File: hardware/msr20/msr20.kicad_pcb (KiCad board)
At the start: 2 copper layers, 0 parts

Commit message: initial board layout; dimensions
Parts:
- added U1: RF-BPF, msr20:RF-BPF, F.Cu at (198.1, 46.3)
- added U2: BGA616, msr20:BGA616, F.Cu at (187.1, 62.9)
- added U3: ADE-1+, msr20:ADE-1+, F.Cu at (189.9, 61.6)
- added U4: AD7478, Package_TO_SOT_SMD:SOT-23-6, F.Cu at (182.3, 63.3)
- added U6: 74LS163, Package_DIP:DIP-16_W7.62mm_LongPads, F.Cu at (181.7, 69.5)
- added U7: CD74HC4046, Package_DIP:DIP-16_W7.62mm_LongPads, F.Cu at (193.3, 69.5)
- added U8: NCP1117-3.3_SOT223, Package_TO_SOT_SMD:SOT-223-3_TabPin2, F.Cu at (209.8, 71.7)
- added U9: NCP1117-5.0_SOT223, Package_TO_SOT_SMD:SOT-223-3_TabPin2, F.Cu at (209.8, 80.0)
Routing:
- added copper zone on B.Cu, net GND
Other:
- board outline added: 120 x 100 mm

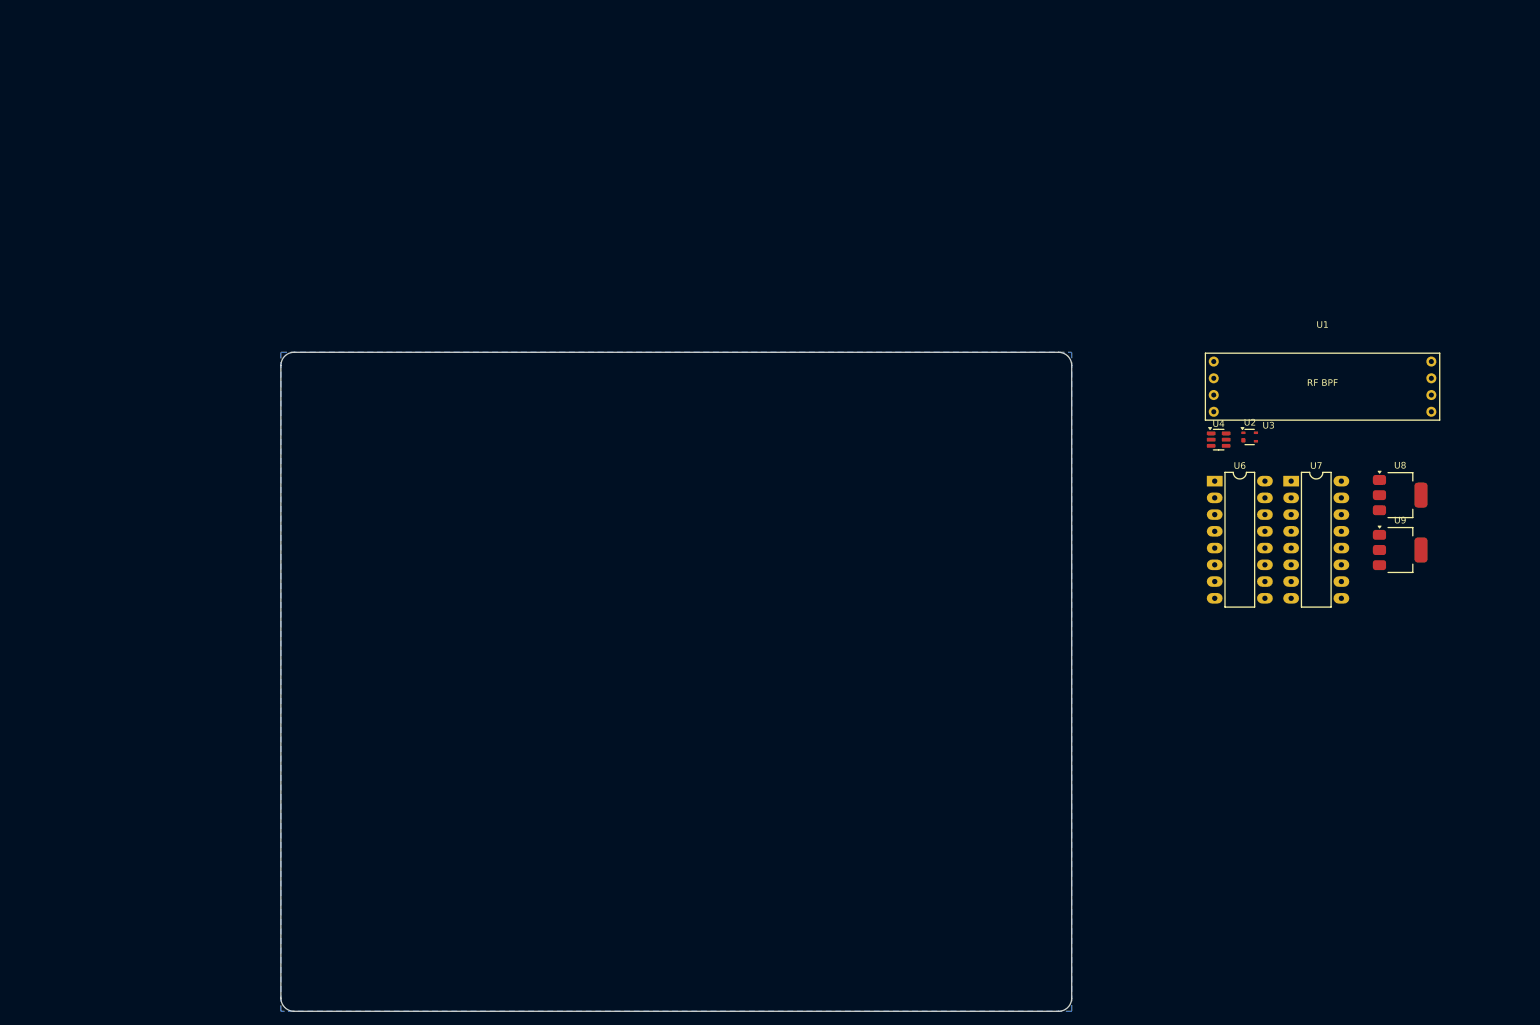
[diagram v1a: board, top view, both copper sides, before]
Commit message: rf-bpf, lna, pll, rf mixer added to pcb
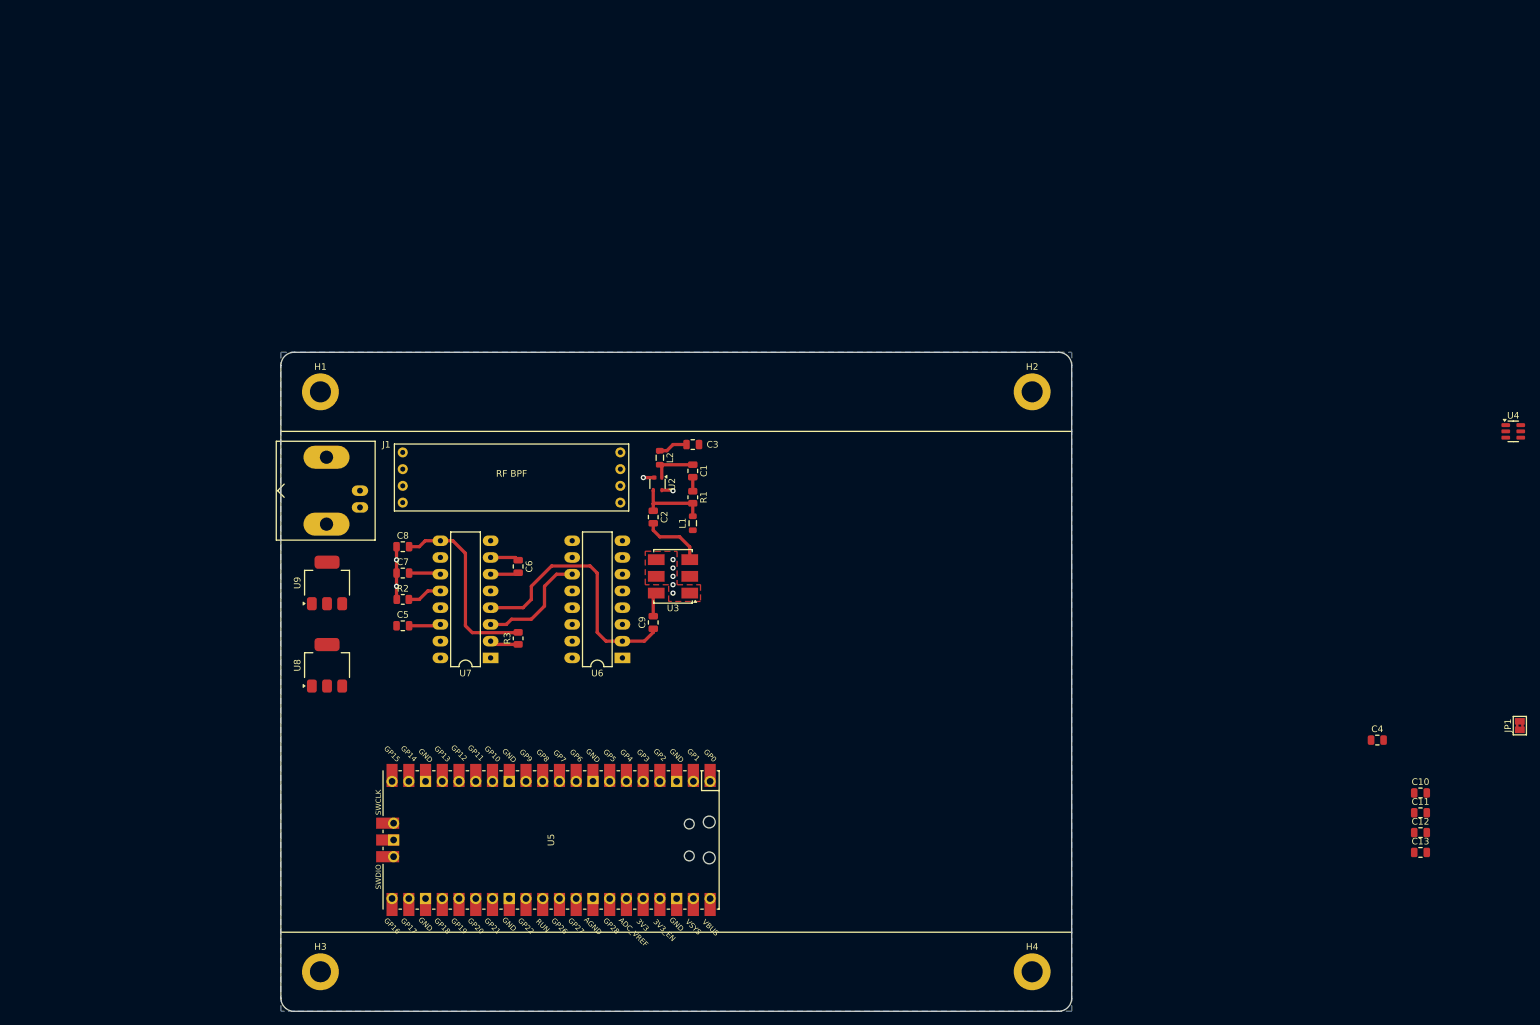
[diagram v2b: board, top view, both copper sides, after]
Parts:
- added C1: 200n, Capacitor_SMD:C_0805_2012Metric, F.Cu at (102.5, 68.0)
- added C10: 1u, Capacitor_SMD:C_0805_2012Metric, F.Cu at (212.9, 116.9)
- added C11: 1u, Capacitor_SMD:C_0805_2012Metric, F.Cu at (212.9, 119.9)
- added C12: 1u, Capacitor_SMD:C_0805_2012Metric, F.Cu at (212.9, 122.9)
- added C13: 1u, Capacitor_SMD:C_0805_2012Metric, F.Cu at (212.9, 125.9)
- added C2: 2.2u, Capacitor_SMD:C_0805_2012Metric, F.Cu at (96.5, 75.0)
- added C3: 1.5p, Capacitor_SMD:C_0805_2012Metric, F.Cu at (102.5, 64.0)
- added C4: C, Capacitor_SMD:C_0805_2012Metric, F.Cu at (206.4, 108.8)
- added C5: 1n, Capacitor_SMD:C_0805_2012Metric, F.Cu at (58.5, 91.5)
- added C6: 47p, Capacitor_SMD:C_0805_2012Metric, F.Cu at (76.0, 82.5)
- added C7: 1n, Capacitor_SMD:C_0805_2012Metric, F.Cu at (58.5, 83.5)
- added C8: 100p, Capacitor_SMD:C_0805_2012Metric, F.Cu at (58.5, 79.5)
- added C9: 1n, Capacitor_SMD:C_0805_2012Metric, F.Cu at (96.5, 91.0)
- added H1: MountingHole_Pad, MountingHole:MountingHole_3.2mm_M3_DIN965_Pad, F.Cu at (46.0, 56.0)
- added H2: MountingHole_Pad, MountingHole:MountingHole_3.2mm_M3_DIN965_Pad, F.Cu at (154.0, 56.0)
- added H3: MountingHole_Pad, MountingHole:MountingHole_3.2mm_M3_DIN965_Pad, F.Cu at (46.0, 144.0)
- added H4: MountingHole_Pad, MountingHole:MountingHole_3.2mm_M3_DIN965_Pad, F.Cu at (154.0, 144.0)
- added J1: Conn_Coaxial, Connector_Coaxial:BNC_Amphenol_B6252HB-NPP3G-50_Horizontal, F.Cu at (52.0, 71.0)
- added JP1: SolderJumper_2_Open, Jumper:SolderJumper-2_P1.3mm_Bridged2Bar_Pad1.0x1.5mm, F.Cu at (228.0, 106.7)
- added L1: 5.1n, Inductor_SMD:L_0805_2012Metric, F.Cu at (102.5, 75.9)
- added L2: 15u, Inductor_SMD:L_0805_2012Metric, F.Cu at (97.5, 66.0)
- added R1: 1.5k, Resistor_SMD:R_0805_2012Metric, F.Cu at (102.5, 72.0)
- added R2: 3.3k, Resistor_SMD:R_0805_2012Metric, F.Cu at (58.5, 87.5)
- added R3: 33k, Resistor_SMD:R_0805_2012Metric, F.Cu at (76.0, 93.4)
- added U5: Pico, MCU_RaspberryPi_and_Boards:RPi_Pico_SMD_TH, F.Cu at (81.0, 124.0)
- U3: footprint msr20:ADE-1+ -> RF_Mini-Circuits:Mini-Circuits_CD636_H4.11mm
- moved U8 164.9 mm to (47.0, 97.5), turned to 90 degrees
- moved U9 162.9 mm to (47.0, 85.0), turned to 90 degrees
- moved U7 124.4 mm to (71.8, 96.4), turned to 180 degrees
- moved U1 123.8 mm to (75.0, 60.1)
- moved U6 93.8 mm to (91.8, 96.4), turned to 180 degrees
- moved U3 93.1 mm to (99.5, 84.0), turned to 180 degrees
- moved U2 90.2 mm to (97.1, 70.0), turned to -90 degrees
- moved U4 44.7 mm to (227.0, 62.0)
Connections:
- net RF-IN renamed Net-(J1-In)
- U4 pad 3: Net-(U4-VIN) -> unconnected-(U4-VIN-Pad3)
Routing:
- net Net-(U6-CLK): track 0.00 -> 39.6 mm
- net Net-(U7-VCO-I): track 0.00 -> 29.2 mm
- net Net-(U6-Qd): track 0.00 -> 17.3 mm
- net GND: track 0.00 -> 11.4 mm, vias 0 -> 9
- net Net-(U2-OUT): track 0.00 -> 11.1 mm
- net Net-(U3-RF): track 0.00 -> 9.56 mm
- net Net-(U2-IN): track 0.00 -> 7.08 mm
- net Net-(U7-R2): track 0.00 -> 5.32 mm
- net Net-(U7-SIG): track 0.00 -> 4.84 mm
- net Net-(U7-R1): track 0.00 -> 4.83 mm
- net Net-(C3-Pad1): track 0.00 -> 4.80 mm
- net Net-(U7-PC1): track 0.00 -> 4.38 mm
- net Net-(U7-C1B): track 0.00 -> 4.35 mm
- net Net-(U7-C1A): track 0.00 -> 4.27 mm
- net /Phase-Locked Loop/PLL-OUT: track 0.00 -> 3.76 mm
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- added copper zone on F.Cu, net GND

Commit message: add if section to pcb
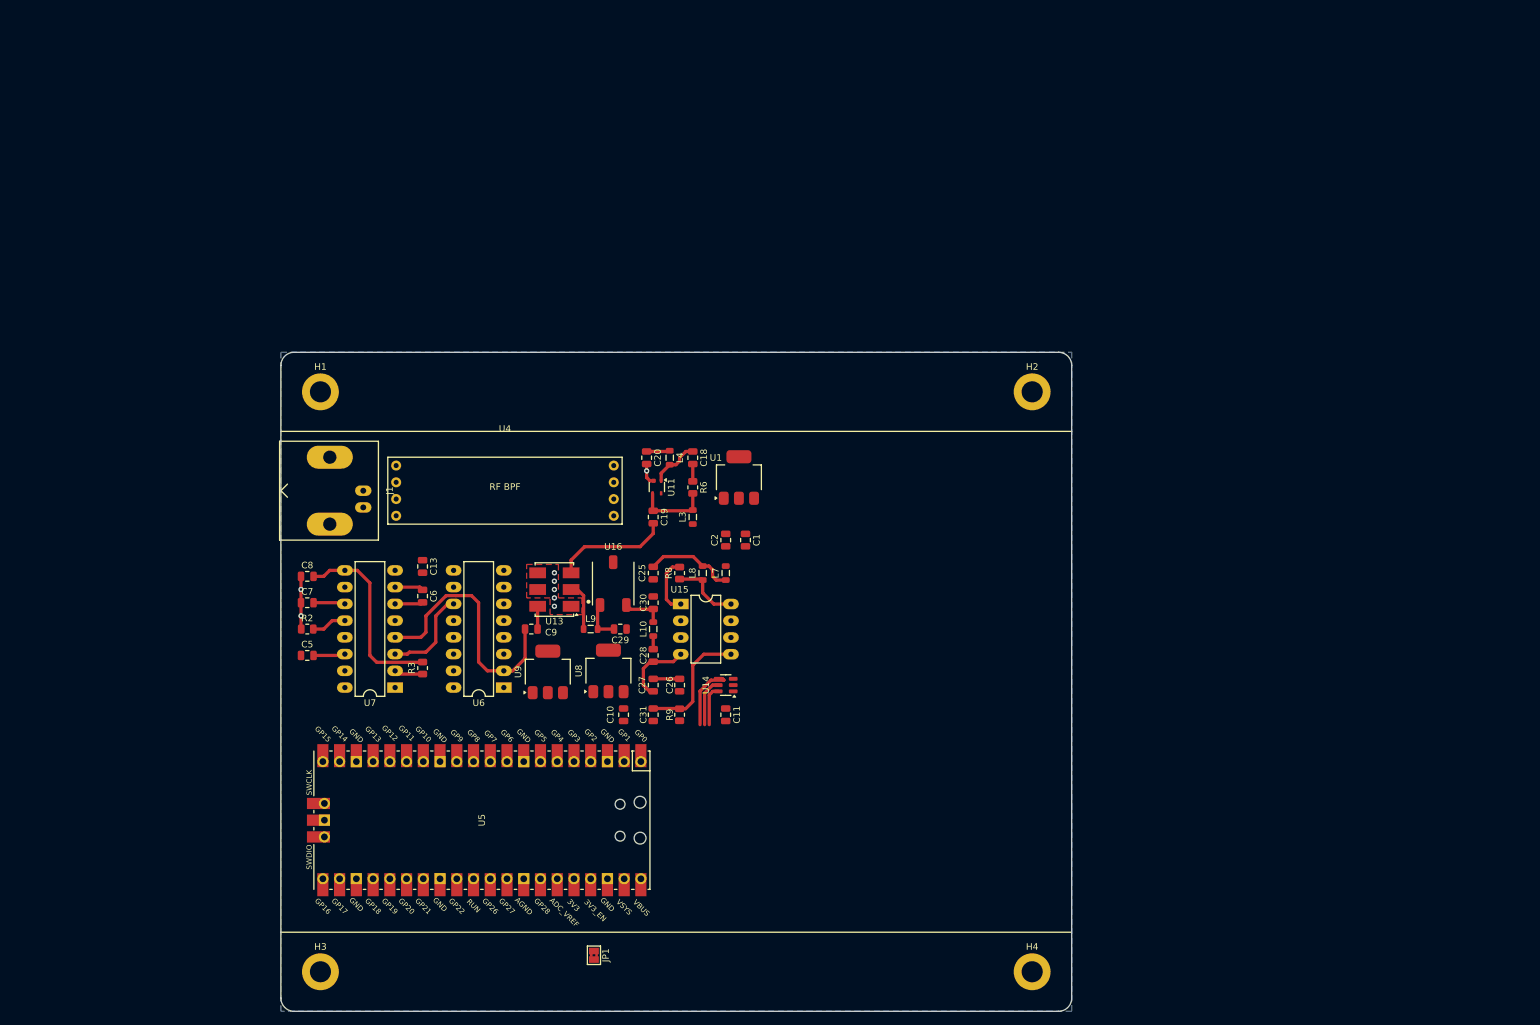
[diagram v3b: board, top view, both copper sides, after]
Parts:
- removed C12: 1u, Capacitor_SMD:C_0805_2012Metric
- removed C3: 1.5p, Capacitor_SMD:C_0805_2012Metric
- removed C4: C, Capacitor_SMD:C_0805_2012Metric
- removed L1: 5.1n, Inductor_SMD:L_0805_2012Metric
- removed L2: 15u, Inductor_SMD:L_0805_2012Metric
- removed R1: 1.5k, Resistor_SMD:R_0805_2012Metric
- removed U2: BGA616, msr20:BGA616
- removed U3: ADE-1+, RF_Mini-Circuits:Mini-Circuits_CD636_H4.11mm
- added C18: 200n, Capacitor_SMD:C_0805_2012Metric, F.Cu at (102.5, 66.0)
- added C19: 2.2u, Capacitor_SMD:C_0805_2012Metric, F.Cu at (96.5, 75.0)
- added C20: 1.5p, Capacitor_SMD:C_0805_2012Metric, F.Cu at (95.5, 66.0)
- added C25: 10n, Capacitor_SMD:C_0805_2012Metric, F.Cu at (96.5, 83.5)
- added C26: 10n, Capacitor_SMD:C_0805_2012Metric, F.Cu at (100.5, 100.5)
- added C27: 100p, Capacitor_SMD:C_0805_2012Metric, F.Cu at (96.5, 100.5)
- added C28: 10n, Capacitor_SMD:C_0805_2012Metric, F.Cu at (96.5, 96.0)
- added C29: 1.2n, Capacitor_SMD:C_0805_2012Metric, F.Cu at (91.5, 92.0)
- added C30: 1.2n, Capacitor_SMD:C_0805_2012Metric, F.Cu at (96.5, 88.0)
- added C31: 10n, Capacitor_SMD:C_0805_2012Metric, F.Cu at (96.5, 105.0)
- added L10: 92m, Inductor_SMD:L_0805_2012Metric, F.Cu at (96.5, 92.0)
- added L3: 5.1n, Inductor_SMD:L_0805_2012Metric, F.Cu at (102.5, 75.0)
- added L4: 15u, Inductor_SMD:L_0805_2012Metric, F.Cu at (99.0, 66.0)
- added L7: 18m, Inductor_SMD:L_0805_2012Metric, F.Cu at (107.5, 83.5)
- added L8: 18m, Inductor_SMD:L_0805_2012Metric, F.Cu at (104.0, 83.5)
- added L9: 92m, Inductor_SMD:L_0805_2012Metric, F.Cu at (87.0, 92.0)
- added R6: 1.5k, Resistor_SMD:R_0805_2012Metric, F.Cu at (102.5, 70.5)
- added R8: 5.1k, Resistor_SMD:R_0805_2012Metric, F.Cu at (100.5, 83.5)
- added R9: 5.1k, Resistor_SMD:R_0805_2012Metric, F.Cu at (100.5, 105.0)
- added U11: BGA616, msr20:BGA616, F.Cu at (97.0, 70.5)
- added U13: ADE-1+, RF_Mini-Circuits:Mini-Circuits_CD636_H4.11mm, F.Cu at (81.5, 86.0)
- added U14: AD7478, Package_TO_SOT_SMD:SOT-23-6, F.Cu at (107.5, 100.5)
- added U15: MC1350, Package_DIP:DIP-8_W7.62mm_LongPads, F.Cu at (100.7, 88.2)
- added U16: LTC455-FU, msr20:LTC455, F.Cu at (90.4, 76.8)
- C1: value 200n -> 1u
- C2: value 2.2u -> 1u
- U1: value RF-BPF -> NCP1117-12_SOT223; footprint msr20:RF-BPF -> Package_TO_SOT_SMD:SOT-223-3_TabPin2
- U4: value AD7478 -> RF-BPF; footprint Package_TO_SOT_SMD:SOT-23-6 -> msr20:RF-BPF
- moved C13 157.5 mm to (61.5, 82.5), turned to -90 degrees
- moved U4 153.0 mm to (74.0, 62.1)
- moved JP1 144.8 mm to (87.5, 141.5), turned to -90 degrees
- moved C10 121.5 mm to (92.0, 105.0), turned to -90 degrees
- moved C11 106.5 mm to (107.5, 105.0), turned to -90 degrees
- moved U8 42.7 mm to (89.7, 98.3)
- moved U9 36.1 mm to (80.5, 98.5)
- moved U1 35.6 mm to (109.5, 69.0), turned to 90 degrees
- moved U6 18.6 mm to (73.8, 100.9)
- moved C9 18.5 mm to (78.0, 92.0), turned to 0 degrees
- moved C5 15.2 mm to (44.0, 96.0)
- moved C6 15.2 mm to (61.5, 87.0)
- moved C7 15.2 mm to (44.0, 88.0)
- moved C8 15.2 mm to (44.0, 84.0)
- moved R2 15.2 mm to (44.0, 92.0)
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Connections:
- C1 pad 1: Net-(U2-IN) -> VIN
- C1 pad 2: Net-(C1-Pad2) -> GND
- C2 pad 1: Net-(U2-OUT) -> +12V
- C2 pad 2: Net-(U3-RF) -> GND
- C5 pad 1: /Phase-Locked Loop/PLL-IN -> PLL-IN
- C9 pad 2: /Phase-Locked Loop/PLL-OUT -> /Phase-Locked Loop/OUT
- U1 pad 1: Net-(J1-In) -> GND
- U1 pad 2: Net-(J1-In) -> +12V
- U1 pad 3: GND -> VIN
- U4 pad 1: +3.3V -> Net-(J1-In)
- U4 pad 2: GND -> Net-(J1-In)
- U4 pad 3: unconnected-(U4-VIN-Pad3) -> GND
- U4 pad 4: ADC-SCK -> GND
- U4 pad 5: ADC-SDA -> GND
- U4 pad 6: ADC-CS -> GND
- U5 pad 12: unconnected-(U5-GPIO9-Pad12) -> PLL-IN
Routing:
- net Net-(U15-AGC): track 0.00 -> 18.5 mm
- net Net-(U13-RF): track 0.00 -> 17.6 mm
- net Net-(U15-VCC): track 0.00 -> 13.7 mm
- net Net-(U11-OUT): track 0.00 -> 11.3 mm
- net Net-(U2-OUT): track 11.1 -> 0.00 mm
- net Net-(U15-IN-): track 0.00 -> 11.0 mm
- net Net-(U14-VIN): track 0.00 -> 10.5 mm
- net ADC-SCK: track 0.00 -> 10.3 mm
- net Net-(U3-RF): track 9.56 -> 0.00 mm
- net Net-(U15-OUT-): track 0.00 -> 8.84 mm
- net Net-(U11-IN): track 0.00 -> 7.60 mm
- net ADC-SDA: track 0.00 -> 7.35 mm
- net /IF Stage/INPUT: track 0.00 -> 7.35 mm
- net Net-(U2-IN): track 7.08 -> 0.00 mm
- net Net-(U16-OUT): track 0.00 -> 6.35 mm
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
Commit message: ground routing
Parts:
- added C12: 1u, Capacitor_SMD:C_0805_2012Metric, F.Cu at (6.78, 9.11)
- added TP1: TestPoint, TestPoint:TestPoint_Pad_D1.0mm, F.Cu at (6.08, 1.02)
- added TP2: TestPoint, TestPoint:TestPoint_Pad_D1.0mm, F.Cu at (6.08, 4.08)
- added TP3: TestPoint, TestPoint:TestPoint_Pad_D1.0mm, F.Cu at (11.1, 1.02)
- added TP4: TestPoint, TestPoint:TestPoint_Pad_D1.0mm, F.Cu at (1.02, 1.02)
- added TP5: TestPoint, TestPoint:TestPoint_Pad_D1.0mm, F.Cu at (1.02, 4.08)
- added TP6: TestPoint, TestPoint:TestPoint_Pad_D1.0mm, F.Cu at (1.02, 7.12)
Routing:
- net GND: track 11.3 -> 29.9 mm, vias 8 -> 10
- net Net-(U15-VCC): track 13.7 -> 31.6 mm
- net +5V: track 0.00 -> 5.34 mm
